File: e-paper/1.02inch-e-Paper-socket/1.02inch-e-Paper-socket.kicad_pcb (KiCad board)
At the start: 2 copper layers, 4 parts, among them J1 Conn_01x06_Pin, J2 Conn_01x03_Pin

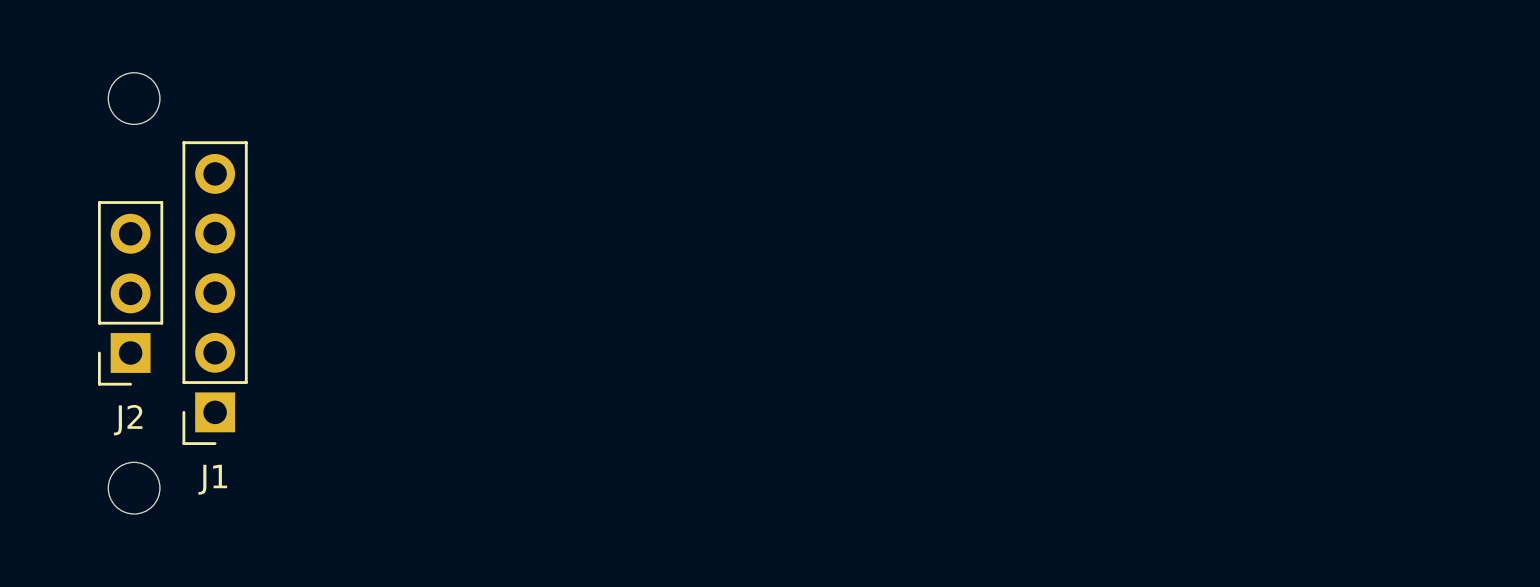
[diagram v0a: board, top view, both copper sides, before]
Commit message: update e-paper boundary
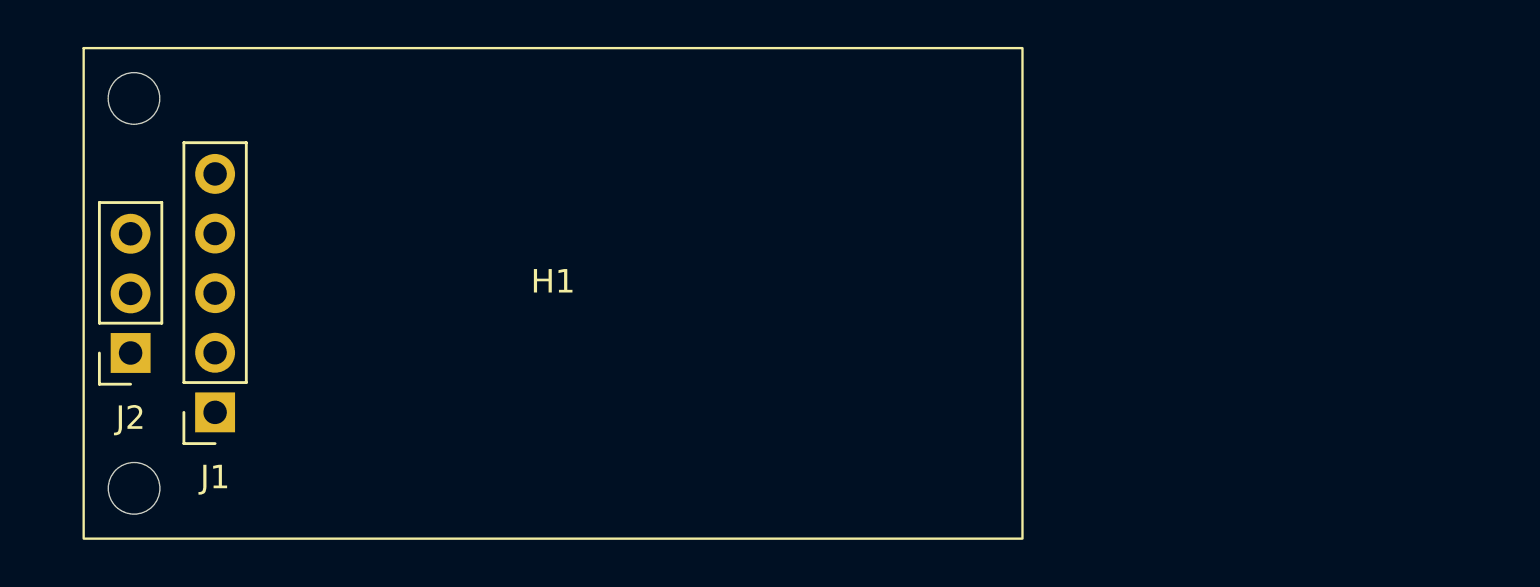
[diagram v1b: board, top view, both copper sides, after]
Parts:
- removed REF** (x2): MountingHole_2.2mm_M2_DIN965, ErgoCai.pretty:MountingHole_2.2mm_M2_DIN965
- added H1: MountingHole, ErgoCai.pretty:e-paper_1.02inch_mount, F.Cu at (20.0, 0.00)
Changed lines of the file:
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@@
 	(net 7 "3.3V")
 	(net 8 "BUSY")
-	(footprint "ErgoCai.pretty:MountingHole_2.2mm_M2_DIN965"
-		(layer "F.Cu")
-		(at 2.15 -8.3)
-		(descr "Mounting Hole 2.2mm, M2, no annular, generated by kicad-footprint-generator mountinghole.py")
-		(tags "mountinghole M2 DIN965")
-		(property "Reference" "REF**"
-			(at 0 -2.85 0)
-			(layer "F.SilkS")
-			(hide yes)
-			(effects
-				(font
-					(size 1 1)
-					(thickness 0.15)
-				)
-			)
-		)
-		(property "Value" "MountingHole_2.2mm_M2_DIN965"
-			(at 0 2.85 0)
-			(layer "F.Fab")
-			(effects
-				(font
-					(size 1 1)
-					(thickness 0.15)
-				)
-			)
-		)
-		(property "Datasheet" ""
-			(at 0 0 0)
-			(layer "F.Fab")
-			(hide yes)
-			(effects
-				(font
-					(size 1.27 1.27)
-					(thickness 0.15)
-				)
-			)
-		)
-		(property "Description" ""
-			(at 0 0 0)
-			(layer "F.Fab")
-			(hide yes)
-			(effects
-				(font
-					(size 1.27 1.27)
-					(thickness 0.15)
-				)
-			)
-		)
-		(attr exclude_from_pos_files exclude_from_bom)
-		(fp_circle
-			(center 0 0)
-			(end 1.9 0)
-			(stroke
-				(width 0.15)
-				(type solid)
-			)
-			(fill no)
-			(layer "Cmts.User")
-		)
-		(fp_circle
-			(center 0 0)
-			(end 2.15 0)
-			(stroke
-				(width 0.05)
-				(type solid)
-			)
-			(fill no)
-			(layer "F.CrtYd")
-		)
-		(pad "" np_thru_hole circle
-			(at 0 0)
-			(size 2.2 2.2)
-			(drill 2.2)
-			(layers "*.Cu" "*.Mask")
-		)
-		(embedded_fonts no)
-	)
 	(footprint "ErgoCai.pretty:PinSocket_1x03_P2.54mm_Vertical"
 		(layer "F.Cu")
@@
 			)
 		)
-		(property "Datasheet" ""
+		(property "Datasheet" "~"
 			(at 0 0 180)
 			(layer "F.Fab")
@@
 			)
 		)
-		(property "Description" ""
+		(property "Description" "Generic connector, single row, 01x03, script generated"
 			(at 0 0 180)
 			(layer "F.Fab")
@@
 		)
 	)
-	(footprint "ErgoCai.pretty:MountingHole_2.2mm_M2_DIN965"
+	(footprint "ErgoCai.pretty:e-paper_1.02inch_mount"
 		(layer "F.Cu")
-		(at 2.15 8.3)
-		(descr "Mounting Hole 2.2mm, M2, no annular, generated by kicad-footprint-generator mountinghole.py")
-		(tags "mountinghole M2 DIN965")
-		(property "Reference" "REF**"
-			(at 0 -2.85 0)
-			(layer "F.SilkS")
+		(at 20 0)
+		(property "Reference" "H1"
+			(at 0 -0.5 0)
+			(unlocked yes)
+			(layer "F.SilkS")
+			(effects
+				(font
+					(size 1 1)
+					(thickness 0.1)
+				)
+			)
+		)
+		(property "Value" "MountingHole"
+			(at 0 1 0)
+			(unlocked yes)
+			(layer "F.Fab")
+			(effects
+				(font
+					(size 1 1)
+					(thickness 0.15)
+				)
+			)
+		)
+		(property "Datasheet" "~"
+			(at 0 0 0)
+			(unlocked yes)
+			(layer "F.Fab")
 			(hide yes)
 			(effects
@@
 			)
 		)
-		(property "Value" "MountingHole_2.2mm_M2_DIN965"
-			(at 0 2.85 0)
-			(layer "F.Fab")
-			(effects
-				(font
-					(size 1 1)
-					(thickness 0.15)
-				)
-			)
-		)
-		(property "Datasheet" ""
+		(property "Description" "Mounting Hole without connection"
 			(at 0 0 0)
+			(unlocked yes)
 			(layer "F.Fab")
 			(hide yes)
 			(effects
 				(font
-					(size 1.27 1.27)
-					(thickness 0.15)
-				)
-			)
-		)
-		(property "Description" ""
-			(at 0 0 0)
-			(layer "F.Fab")
-			(hide yes)
-			(effects
-				(font
-					(size 1.27 1.27)
-					(thickness 0.15)
-				)
-			)
-		)
-		(attr exclude_from_pos_files exclude_from_bom)
+					(size 1 1)
+					(thickness 0.15)
+				)
+			)
+		)
+		(property ki_fp_filters "MountingHole*")
+		(sheetname "/")
+		(sheetfile "1.02inch-e-Paper-socket.kicad_sch")
+		(attr smd exclude_from_bom)
+		(fp_rect
+			(start -20 -10.45)
+			(end 20 10.45)
+			(stroke
+				(width 0.1)
+				(type solid)
+			)
+			(fill no)
+			(layer "F.SilkS")
+		)
 		(fp_circle
-			(center 0 0)
-			(end 1.9 0)
+			(center -17.8562 -8.3058)
+			(end -15.9562 -8.3058)
 			(stroke
 				(width 0.15)
@@
 		)
 		(fp_circle
-			(center 0 0)
-			(end 2.15 0)
-			(stroke
-				(width 0.05)
+			(center -17.8512 8.3058)
+			(end -15.9512 8.3058)
+			(stroke
+				(width 0.15)
 				(type solid)
 			)
 			(fill no)
-			(layer "F.CrtYd")
+			(layer "Cmts.User")
+		)
+		(fp_circle
+			(center -17.8562 -8.3058)
+			(end -15.7062 -8.3058)
+			(stroke
+				(width 0.05)
+				(type solid)
+			)
+			(fill no)
+			(layer "F.CrtYd")
+		)
+		(fp_circle
+			(center -17.8512 8.3058)
+			(end -15.7012 8.3058)
+			(stroke
+				(width 0.05)
+				(type solid)
+			)
+			(fill no)
+			(layer "F.CrtYd")
+		)
+		(fp_text user "${REFERENCE}"
+			(at 0 2.5 0)
+			(unlocked yes)
+			(layer "F.Fab")
+			(effects
+				(font
+					(size 1 1)
+					(thickness 0.15)
+				)
+			)
 		)
 		(pad "" np_thru_hole circle
-			(at 0 0)
+			(at -17.8562 -8.3058)
+			(size 2.2 2.2)
+			(drill 2.2)
+			(layers "*.Cu" "*.Mask")
+		)
+		(pad "" np_thru_hole circle
+			(at -17.8512 8.3058)
 			(size 2.2 2.2)
 			(drill 2.2)
@@
 			)
 		)
-		(property "Datasheet" ""
+		(property "Datasheet" "~"
 			(at 0 0 180)
 			(layer "F.Fab")
@@
 			)
 		)
-		(property "Description" ""
+		(property "Description" "Generic connector, single row, 01x05, script generated"
 			(at 0 0 180)
 			(layer "F.Fab")
@@
 		)
 	)
-	(gr_rect
-		(start 0 -10.45)
-		(end 40 10.45)
-		(stroke
-			(width 0.1)
-			(type solid)
-		)
-		(fill no)
-		(layer "F.CrtYd")
-	)
 	(embedded_fonts no)

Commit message: update reference in joystick and e-paper
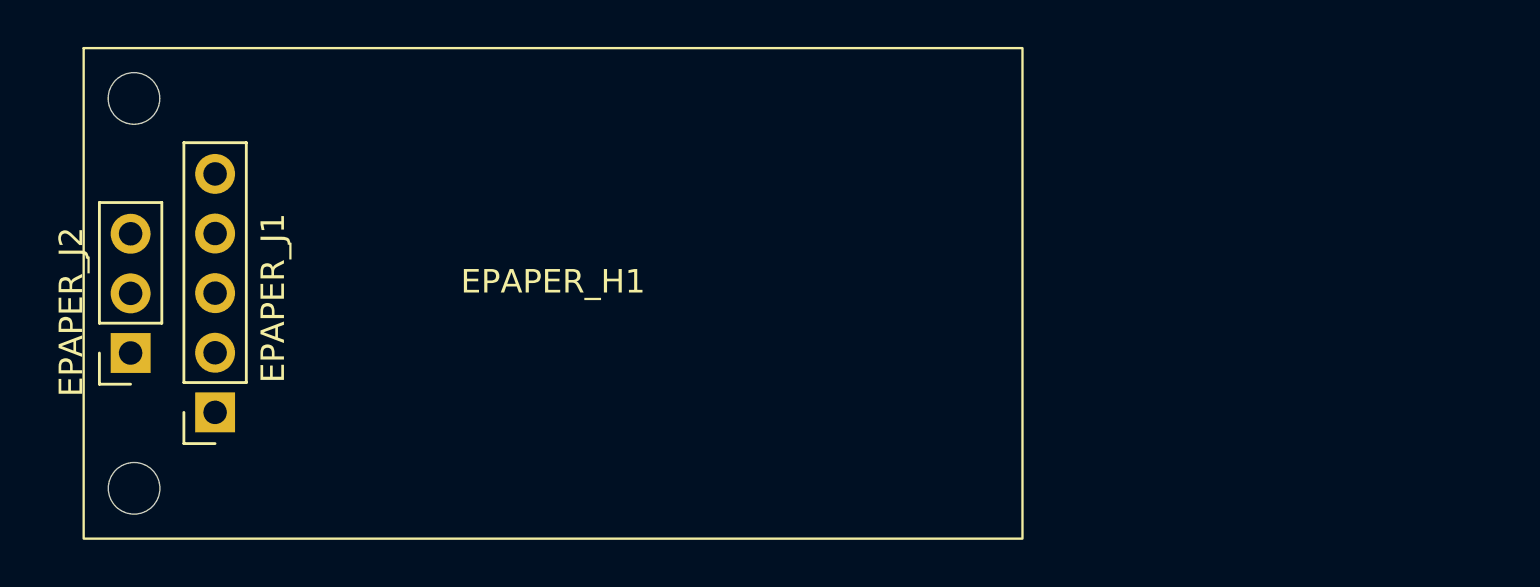
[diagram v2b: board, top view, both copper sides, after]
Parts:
- removed H1: MountingHole, ErgoCai.pretty:e-paper_1.02inch_mount
- added EPAPER_H1: MountingHole, ErgoCai.pretty:e-paper_1.02inch_mount, F.Cu at (20.0, 0.00)
- renumbered J1 to EPAPER_J1, J2 to EPAPER_J2
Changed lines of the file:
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@@
 		(descr "Through hole straight socket strip, 1x03, 2.54mm pitch, single row (from Kicad 4.0.7), script generated")
 		(tags "Through hole socket strip THT 1x03 2.54mm single row")
-		(property "Reference" "J2"
-			(at 0 -2.77 180)
+		(property "Reference" "EPAPER_J2"
+			(at 2.53 1.75 270)
 			(layer "F.SilkS")
 			(effects
@@
 		(layer "F.Cu")
 		(at 20 0)
-		(property "Reference" "H1"
+		(property "Reference" "EPAPER_H1"
 			(at 0 -0.5 0)
 			(unlocked yes)
@@
 		(descr "Through hole straight socket strip, 1x05, 2.54mm pitch, single row (from Kicad 4.0.7), script generated")
 		(tags "Through hole socket strip THT 1x05 2.54mm single row")
-		(property "Reference" "J1"
-			(at 0 -2.77 180)
-			(layer "F.SilkS")
-			(effects
+		(property "Reference" "EPAPER_J1"
+			(at -2.47 4.87 90)
+			(layer "F.SilkS")
+			(effects

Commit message: update e-paper
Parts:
- moved EPAPER_J1 10.2 mm to (5.60, -5.08), turned to 0 degrees
- moved EPAPER_H1 10.0 mm to (30.0, 0.00)
- moved EPAPER_J2 5.09 mm to (2.00, -2.55), turned to 0 degrees

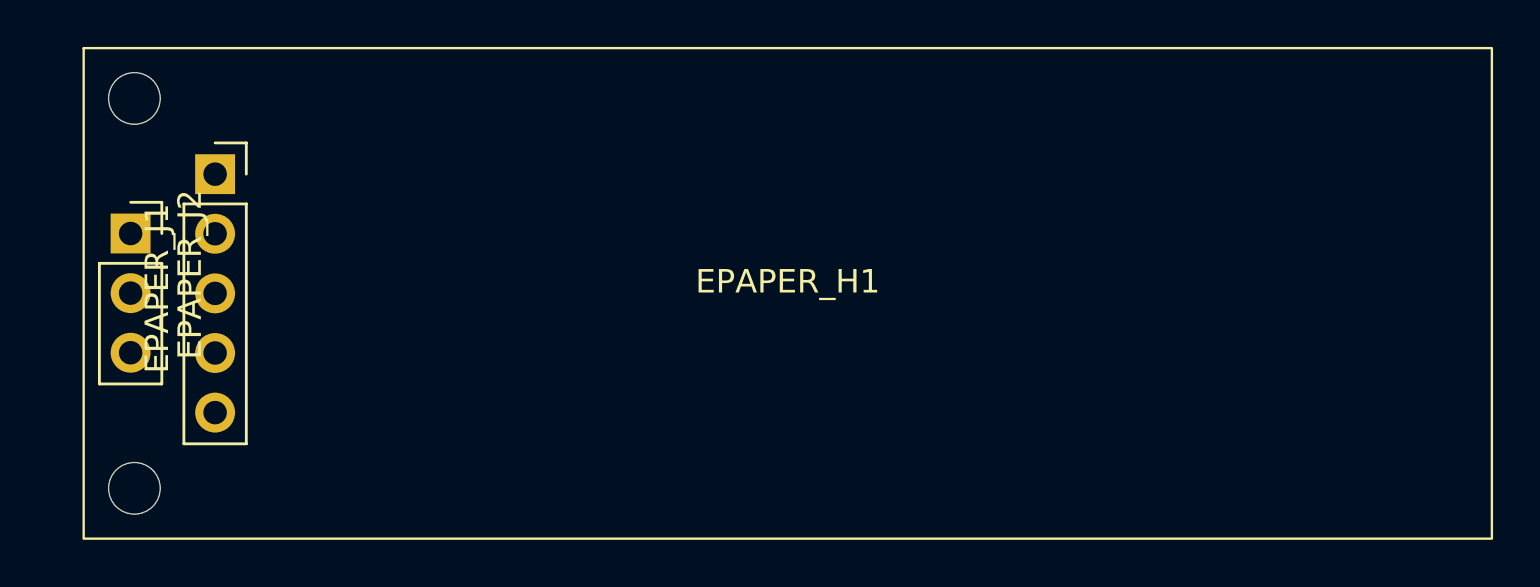
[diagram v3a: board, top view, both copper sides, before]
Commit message: use 10pin connector socket instead of 9
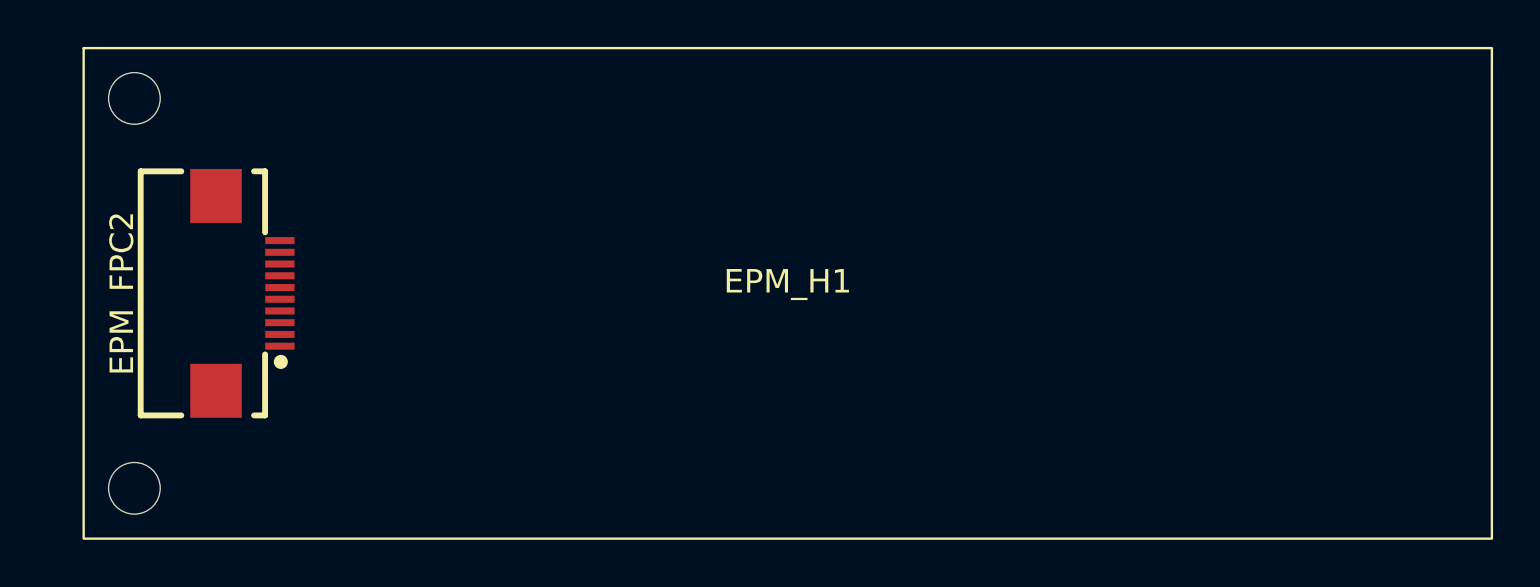
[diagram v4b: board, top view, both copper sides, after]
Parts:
- removed EPAPER_J1: Conn_01x06_Pin, ErgoCai.pretty:PinSocket_1x05_P2.54mm_Vertical
- removed EPAPER_J2: Conn_01x03_Pin, ErgoCai.pretty:PinSocket_1x03_P2.54mm_Vertical
- added EPM_FPC2: AFD01-S10FCA-00, ErgoCai.pretty:FPC-SMD_10P-P0.50_JS_AFD01-S10FCA-00, F.Cu at (7.00, 0.00)
- renumbered EPAPER_H1 to EPM_H1

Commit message: updat e-paper module
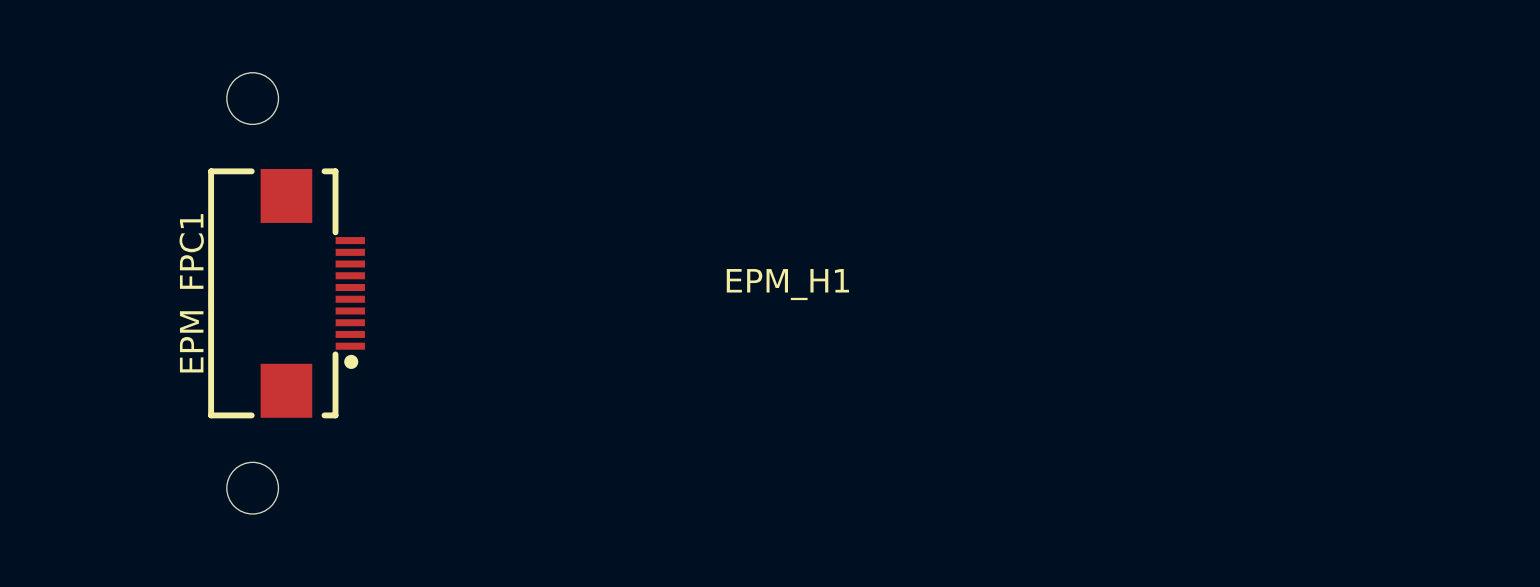
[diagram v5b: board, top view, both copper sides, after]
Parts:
- moved EPM_FPC1 3.00 mm to (10.0, 0.00)
- renumbered EPM_FPC2 to EPM_FPC1
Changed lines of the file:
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@@
 	(net 0 "")
 	(net 1 "EP_CS")
-	(net 2 "unconnected-(EPM_FPC2-Pad10)")
+	(net 2 "unconnected-(EPM_FPC1-Pad10)")
 	(net 3 "EP_BUSY")
 	(net 4 "EP_CLK")
@@
 	(footprint "ErgoCai.pretty:FPC-SMD_10P-P0.50_JS_AFD01-S10FCA-00"
 		(layer "F.Cu")
-		(at 7 0 90)
-		(property "Reference" "EPM_FPC2"
+		(at 10 0 90)
+		(property "Reference" "EPM_FPC1"
 			(at 0 -5.36 90)
 			(layer "F.SilkS")
@@
 			(size 0.3 1.25)
 			(layers "F.Cu" "F.Mask" "F.Paste")
-			(net 2 "unconnected-(EPM_FPC2-Pad10)")
+			(net 2 "unconnected-(EPM_FPC1-Pad10)")
 			(pinfunction "10")
 			(pintype "unspecified+no_connect")
@@
 		(sheetfile "1.02inch-e-Paper-socket.kicad_sch")
 		(attr smd exclude_from_bom)
+		(fp_circle
+			(center -22.8 -8.3)
+			(end -20.9 -8.3)
+			(stroke
+				(width 0.15)
+				(type solid)
+			)
+			(fill no)
+			(layer "Cmts.User")
+		)
+		(fp_circle
+			(center -22.8 8.3)
+			(end -20.9 8.3)
+			(stroke
+				(width 0.15)
+				(type solid)
+			)
+			(fill no)
+			(layer "Cmts.User")
+		)
 		(fp_rect
-			(start -30 -10.45)
-			(end 30 10.45)
+			(start -25 -10.45)
+			(end 25 10.45)
 			(stroke
 				(width 0.1)
@@
 			)
 			(fill no)
-			(layer "F.SilkS")
-		)
-		(fp_circle
-			(center -27.8384 -8.3058)
-			(end -25.9384 -8.3058)
-			(stroke
-				(width 0.15)
-				(type solid)
-			)
-			(fill no)
-			(layer "Cmts.User")
-		)
-		(fp_circle
-			(center -27.8384 8.3058)
-			(end -25.9384 8.3058)
-			(stroke
-				(width 0.15)
-				(type solid)
-			)
-			(fill no)
-			(layer "Cmts.User")
-		)
-		(fp_circle
-			(center -27.8384 -8.3058)
-			(end -25.6884 -8.3058)
+			(layer "F.CrtYd")
+		)
+		(fp_circle
+			(center -22.8 -8.3)
+			(end -20.65 -8.3)
 			(stroke
 				(width 0.05)
@@
 		)
 		(fp_circle
-			(center -27.8384 8.3058)
-			(end -25.6884 8.3058)
+			(center -22.8 8.3)
+			(end -20.65 8.3)
 			(stroke
 				(width 0.05)
@@
 		)
 		(pad "" np_thru_hole circle
-			(at -27.8384 -8.3058)
+			(at -22.8 -8.3)
 			(size 2.2 2.2)
 			(drill 2.2)
@@
 		)
 		(pad "" np_thru_hole circle
-			(at -27.8384 8.3058)
+			(at -22.8 8.3)
 			(size 2.2 2.2)
 			(drill 2.2)
